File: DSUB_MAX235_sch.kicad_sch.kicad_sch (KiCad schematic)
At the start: 2 parts

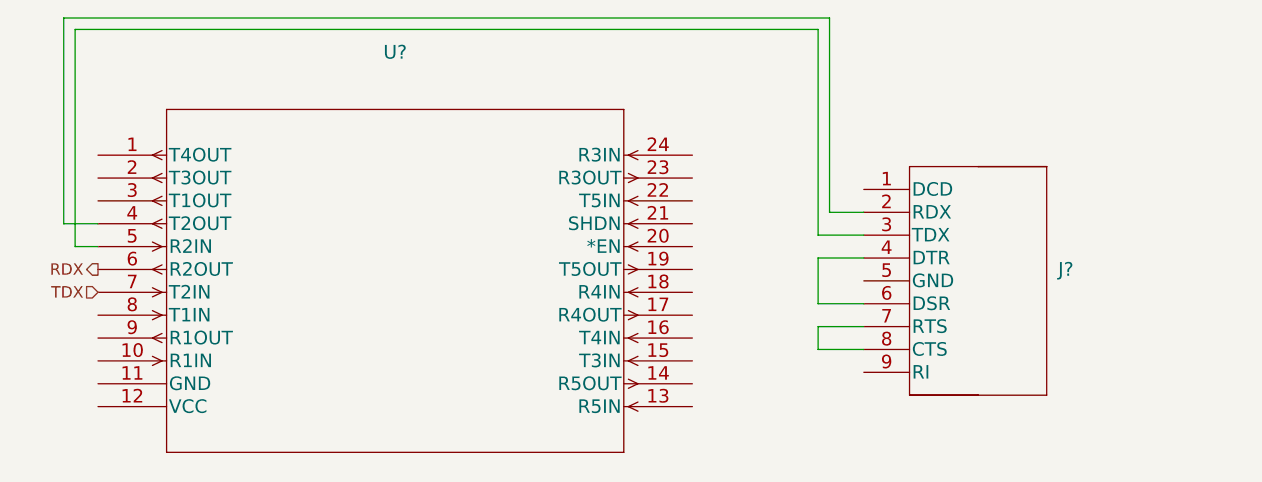
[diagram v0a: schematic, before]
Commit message: Added Clock Circuit
Moved the main circuit to the right and added a simple clock generator circuit to the left of the 8086. Still need to wire reset switch
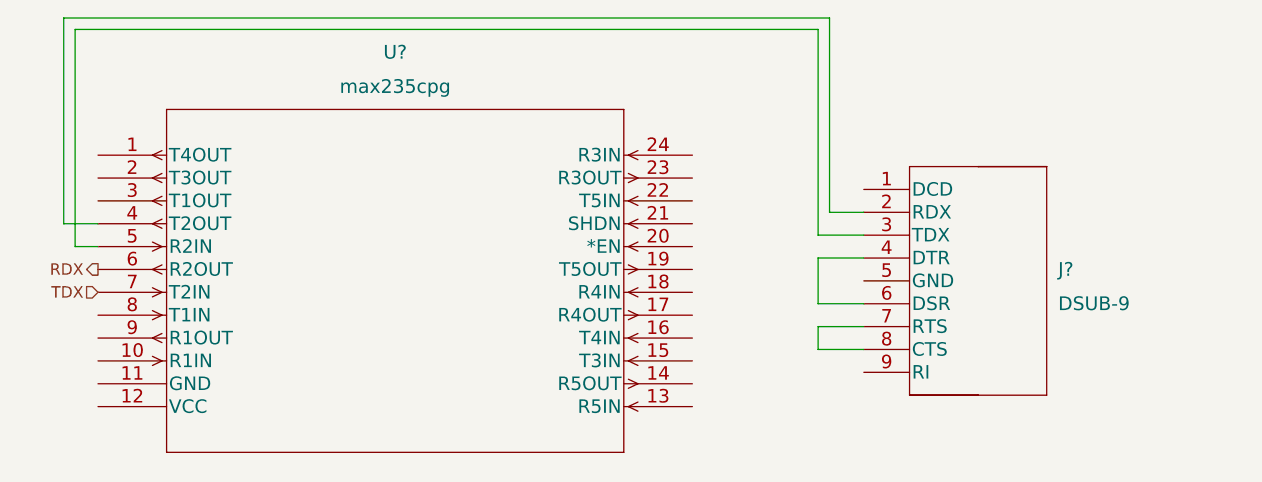
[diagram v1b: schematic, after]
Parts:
- J?: value (none) -> DSUB-9; footprint (none) -> DSUB-9
- U?: value (none) -> max235cpg; footprint (none) -> max235cpg
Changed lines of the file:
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@@
       (effects (font (size 1.524 1.524)))
     )
-    (property "Value" "" (id 1) (at 132.08 59.69 0)
+    (property "Value" "max235cpg" (id 1) (at 132.08 59.69 0)
       (effects (font (size 1.524 1.524)))
     )
-    (property "Footprint" "" (id 2) (at 132.08 61.214 0)
+    (property "Footprint" "max235cpg" (id 2) (at 132.08 61.214 0)
       (effects (font (size 1.524 1.524)) hide)
     )
@@
       (effects (font (size 1.524 1.524)) (justify left))
     )
-    (property "Value" "" (id 1) (at 205.74 83.82 0)
+    (property "Value" "DSUB-9" (id 1) (at 205.74 83.82 0)
       (effects (font (size 1.524 1.524)) (justify left))
     )
-    (property "Footprint" "" (id 2) (at 199.39 80.264 0)
+    (property "Footprint" "DSUB-9" (id 2) (at 199.39 80.264 0)
       (effects (font (size 1.524 1.524)) hide)
     )

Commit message: Wired Push Buttons and added footprints
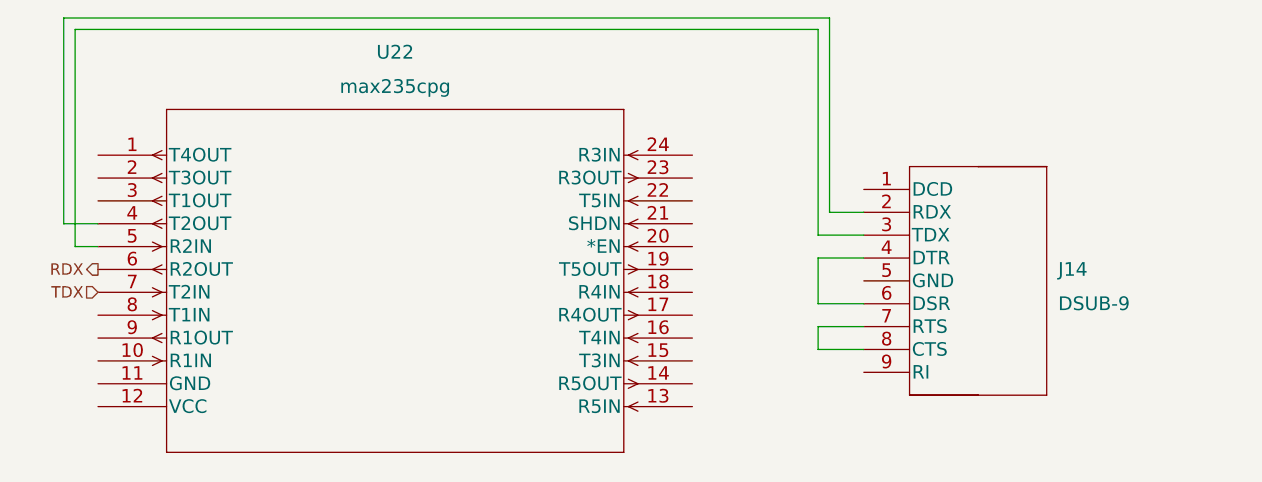
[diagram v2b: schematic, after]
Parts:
- J14: renamed from J?; footprint DSUB-9 -> (none)
- U22: renamed from U?; footprint max235cpg -> (none)
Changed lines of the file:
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@@
   (symbol (lib_id "max235cpg:max235cpg") (at 99.06 67.31 0) (unit 1)
     (in_bom yes) (on_board yes) (fields_autoplaced)
-    (property "Reference" "U?" (id 0) (at 132.08 55.88 0)
+    (property "Reference" "U22" (id 0) (at 132.08 55.88 0)
       (effects (font (size 1.524 1.524)))
     )
@@
       (effects (font (size 1.524 1.524)))
     )
-    (property "Footprint" "max235cpg" (id 2) (at 132.08 61.214 0)
+    (property "Footprint" "" (id 2) (at 132.08 61.214 0)
       (effects (font (size 1.524 1.524)) hide)
     )
@@
   (symbol (lib_id "DSUB-9:DSUB-9") (at 184.15 71.12 0) (unit 1)
     (in_bom yes) (on_board yes) (fields_autoplaced)
-    (property "Reference" "J?" (id 0) (at 205.74 80.01 0)
+    (property "Reference" "J14" (id 0) (at 205.74 80.01 0)
       (effects (font (size 1.524 1.524)) (justify left))
     )
@@
       (effects (font (size 1.524 1.524)) (justify left))
     )
-    (property "Footprint" "DSUB-9" (id 2) (at 199.39 80.264 0)
+    (property "Footprint" "" (id 2) (at 199.39 80.264 0)
       (effects (font (size 1.524 1.524)) hide)
     )

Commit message: Added power and ground to chips
Added power and ground to chips as well as checked and added all labels for pins off of busses
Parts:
- J14: footprint (none) -> parts:DSUB-9
- U22: footprint (none) -> parts:max235cpg
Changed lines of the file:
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@@
       (effects (font (size 1.524 1.524)))
     )
-    (property "Footprint" "" (id 2) (at 132.08 61.214 0)
+    (property "Footprint" "parts:max235cpg" (id 2) (at 132.08 61.214 0)
       (effects (font (size 1.524 1.524)) hide)
     )
@@
       (effects (font (size 1.524 1.524)) (justify left))
     )
-    (property "Footprint" "" (id 2) (at 199.39 80.264 0)
+    (property "Footprint" "parts:DSUB-9" (id 2) (at 199.39 80.264 0)
       (effects (font (size 1.524 1.524)) hide)
     )

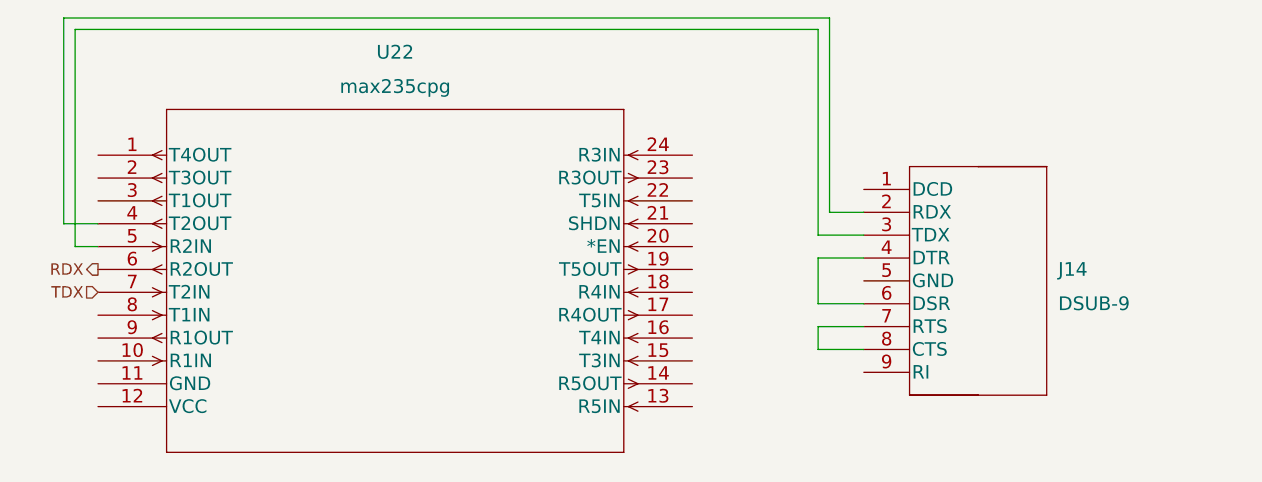
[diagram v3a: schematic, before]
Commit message: Enabled inputs on the max235
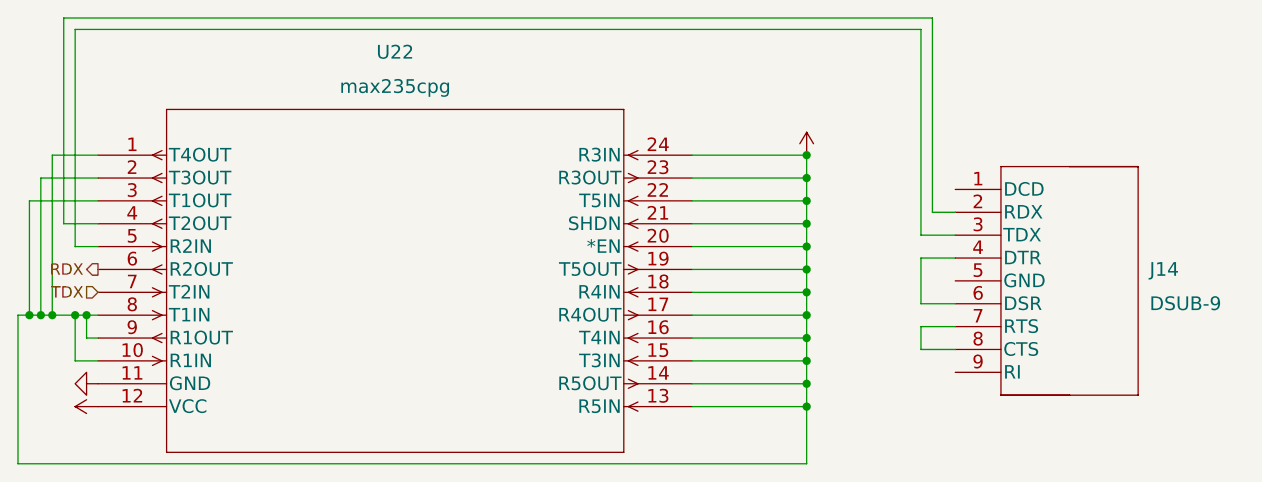
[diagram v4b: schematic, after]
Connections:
- net +5V: now reaches U22.1 (T4OUT)
- net +5V: now also U22.10 (R1IN), U22.12 (VCC), U22.13 (R5IN), U22.14 (R5OUT), U22.15 (T3IN), U22.16 (T4IN), U22.17 (R4OUT), U22.18 (R4IN), U22.19 (T5OUT), U22.2 (T3OUT), U22.20 (*EN), U22.21 (SHDN), U22.22 (T5IN), U22.23 (R3OUT), U22.24 (R3IN), U22.3 (T1OUT), U22.8 (T1IN), U22.9 (R1OUT)
- net GND: now reaches U22.11 (GND)
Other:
- moved on the sheet: J14

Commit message: Updated PCB
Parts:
- J14: value DSUB-9 -> (none); footprint parts:DSUB-9 -> (none)
- U22: value max235cpg -> (none); footprint parts:max235cpg -> (none)
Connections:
- net +5V: no longer U22.20 (*EN)
- net GND: now also U22.20 (*EN)
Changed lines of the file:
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@@
   (junction (at 177.8 72.39) (diameter 0) (color 0 0 0 0)
   )
-  (junction (at 177.8 77.47) (diameter 0) (color 0 0 0 0)
-  )
   (junction (at 96.52 85.09) (diameter 0) (color 0 0 0 0)
   )
@@
     (stroke (width 0) (type default) (color 0 0 0 0))
   )
-  (wire (pts (xy 165.1 77.47) (xy 177.8 77.47))
-    (stroke (width 0) (type default) (color 0 0 0 0))
-  )
   (wire (pts (xy 190.5 76.2) (xy 194.31 76.2))
     (stroke (width 0) (type default) (color 0 0 0 0))
   )
-  (wire (pts (xy 177.8 77.47) (xy 177.8 80.01))
-    (stroke (width 0) (type default) (color 0 0 0 0))
-  )
   (wire (pts (xy 99.06 74.93) (xy 95.25 74.93))
     (stroke (width 0) (type default) (color 0 0 0 0))
@@
     (stroke (width 0) (type default) (color 0 0 0 0))
   )
-  (wire (pts (xy 177.8 74.93) (xy 177.8 77.47))
+  (wire (pts (xy 177.8 74.93) (xy 177.8 80.01))
     (stroke (width 0) (type default) (color 0 0 0 0))
   )
@@
     (effects (font (size 1.27 1.27)) (justify right))
   )
+  (symbol (lib_id "power:GND") (at 165.1 77.47 90) (unit 1)
+    (in_bom yes) (on_board yes) (fields_autoplaced)
+    (property "Reference" "#PWR0133" (id 0) (at 171.45 77.47 0)
+      (effects (font (size 1.27 1.27)) hide)
+    )
+    (property "Value" "" (id 1) (at 168.91 77.4699 90)
+      (effects (font (size 1.27 1.27)) (justify right))
+    )
+    (property "Footprint" "" (id 2) (at 165.1 77.47 0)
+      (effects (font (size 1.27 1.27)) hide)
+    )
+    (property "Datasheet" "" (id 3) (at 165.1 77.47 0)
+      (effects (font (size 1.27 1.27)) hide)
+    )
+    (pin "1")
+  )
   (symbol (lib_id "power:+5V") (at 177.8 67.31 0) (unit 1)
     (in_bom yes) (on_board yes) (fields_autoplaced)
-    (property "Reference" "#PWR?" (id 0) (at 177.8 71.12 0)
+    (property "Reference" "#PWR0128" (id 0) (at 177.8 71.12 0)
       (effects (font (size 1.27 1.27)) hide)
     )
@@
       (effects (font (size 1.524 1.524)))
     )
-    (property "Value" "max235cpg" (id 1) (at 132.08 59.69 0)
+    (property "Value" "" (id 1) (at 132.08 59.69 0)
       (effects (font (size 1.524 1.524)))
     )
-    (property "Footprint" "parts:max235cpg" (id 2) (at 132.08 61.214 0)
+    (property "Footprint" "" (id 2) (at 132.08 61.214 0)
       (effects (font (size 1.524 1.524)) hide)
     )
@@
       (effects (font (size 1.524 1.524)) (justify left))
     )
-    (property "Value" "DSUB-9" (id 1) (at 215.9 83.82 0)
+    (property "Value" "" (id 1) (at 215.9 83.82 0)
       (effects (font (size 1.524 1.524)) (justify left))
     )
-    (property "Footprint" "parts:DSUB-9" (id 2) (at 209.55 80.264 0)
+    (property "Footprint" "" (id 2) (at 209.55 80.264 0)
       (effects (font (size 1.524 1.524)) hide)
     )
@@
   (symbol (lib_id "power:+5V") (at 99.06 95.25 90) (unit 1)
     (in_bom yes) (on_board yes) (fields_autoplaced)
-    (property "Reference" "#PWR?" (id 0) (at 102.87 95.25 0)
+    (property "Reference" "#PWR0129" (id 0) (at 102.87 95.25 0)
       (effects (font (size 1.27 1.27)) hide)
     )
@@
   (symbol (lib_id "power:GND") (at 99.06 92.71 270) (unit 1)
     (in_bom yes) (on_board yes) (fields_autoplaced)
-    (property "Reference" "#PWR?" (id 0) (at 92.71 92.71 0)
-      (effects (font (size 1.27 1.27)) hide)
-    )
+    (property "Reference" "#PWR0130" (id 0) (at 92.71 92.71 0)
+      (effects (font (size 1.27 1.27)) hide)
+    )

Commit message: PCB wiring
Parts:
- J14: value (none) -> DSUB-9; footprint (none) -> parts:DSUB-9
- U22: value (none) -> max235cpg; footprint (none) -> parts:max235cpg
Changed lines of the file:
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@@
       (effects (font (size 1.27 1.27)) hide)
     )
-    (property "Value" "" (id 1) (at 168.91 77.4699 90)
+    (property "Value" "GND" (id 1) (at 168.91 77.4699 90)
       (effects (font (size 1.27 1.27)) (justify right))
     )
@@
       (effects (font (size 1.27 1.27)) hide)
     )
-    (property "Value" "" (id 1) (at 177.8 62.23 0))
+    (property "Value" "+5V" (id 1) (at 177.8 62.23 0))
     (property "Footprint" "" (id 2) (at 177.8 67.31 0)
       (effects (font (size 1.27 1.27)) hide)
@@
       (effects (font (size 1.524 1.524)))
     )
-    (property "Value" "" (id 1) (at 132.08 59.69 0)
+    (property "Value" "max235cpg" (id 1) (at 132.08 59.69 0)
       (effects (font (size 1.524 1.524)))
     )
-    (property "Footprint" "" (id 2) (at 132.08 61.214 0)
+    (property "Footprint" "parts:max235cpg" (id 2) (at 132.08 61.214 0)
       (effects (font (size 1.524 1.524)) hide)
     )
@@
       (effects (font (size 1.524 1.524)) (justify left))
     )
-    (property "Value" "" (id 1) (at 215.9 83.82 0)
+    (property "Value" "DSUB-9" (id 1) (at 215.9 83.82 0)
       (effects (font (size 1.524 1.524)) (justify left))
     )
-    (property "Footprint" "" (id 2) (at 209.55 80.264 0)
+    (property "Footprint" "parts:DSUB-9" (id 2) (at 209.55 80.264 0)
       (effects (font (size 1.524 1.524)) hide)
     )
@@
       (effects (font (size 1.27 1.27)) hide)
     )
-    (property "Value" "" (id 1) (at 95.25 95.2499 90)
+    (property "Value" "+5V" (id 1) (at 95.25 95.2499 90)
       (effects (font (size 1.27 1.27)) (justify left))
     )
@@
       (effects (font (size 1.27 1.27)) hide)
     )
-    (property "Value" "" (id 1) (at 95.25 92.7099 90)
+    (property "Value" "GND" (id 1) (at 95.25 92.7099 90)
       (effects (font (size 1.27 1.27)) (justify right))
     )
